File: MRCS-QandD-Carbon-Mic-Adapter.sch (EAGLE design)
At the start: 4 parts

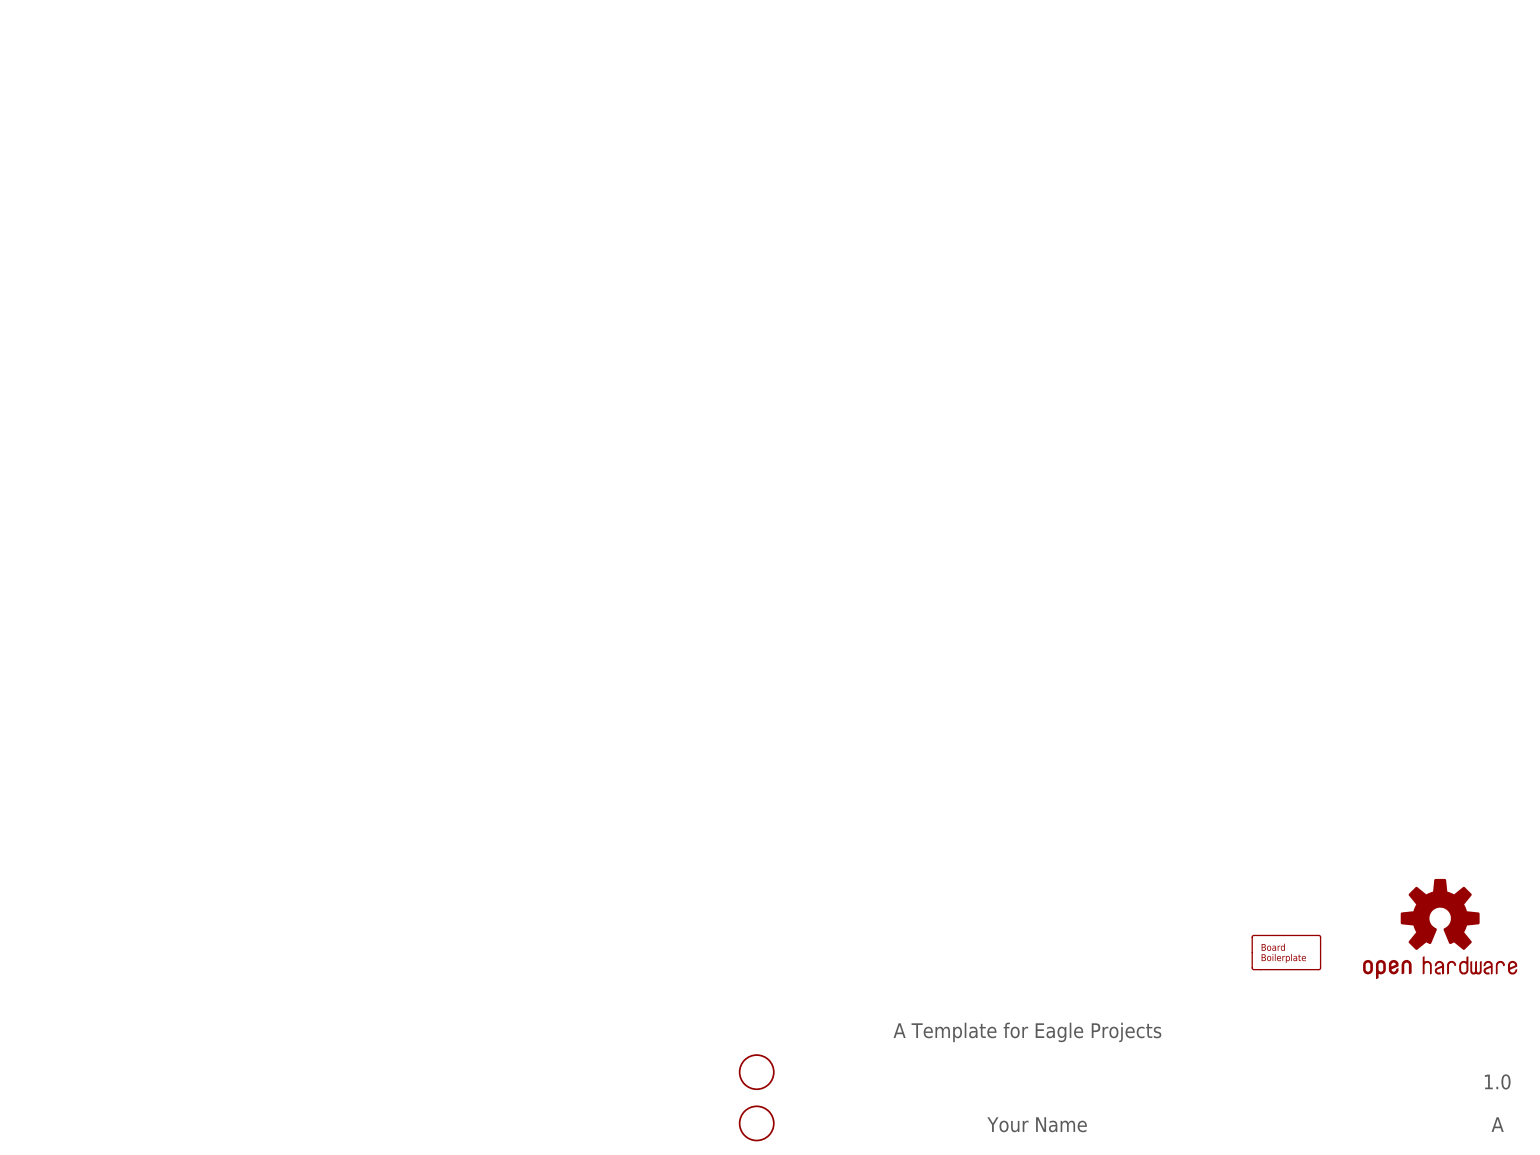
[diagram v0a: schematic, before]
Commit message: Initial design sent to PCB Fab on 1/2/22
First pass board, easier to make the PCB than fool with a bread board.
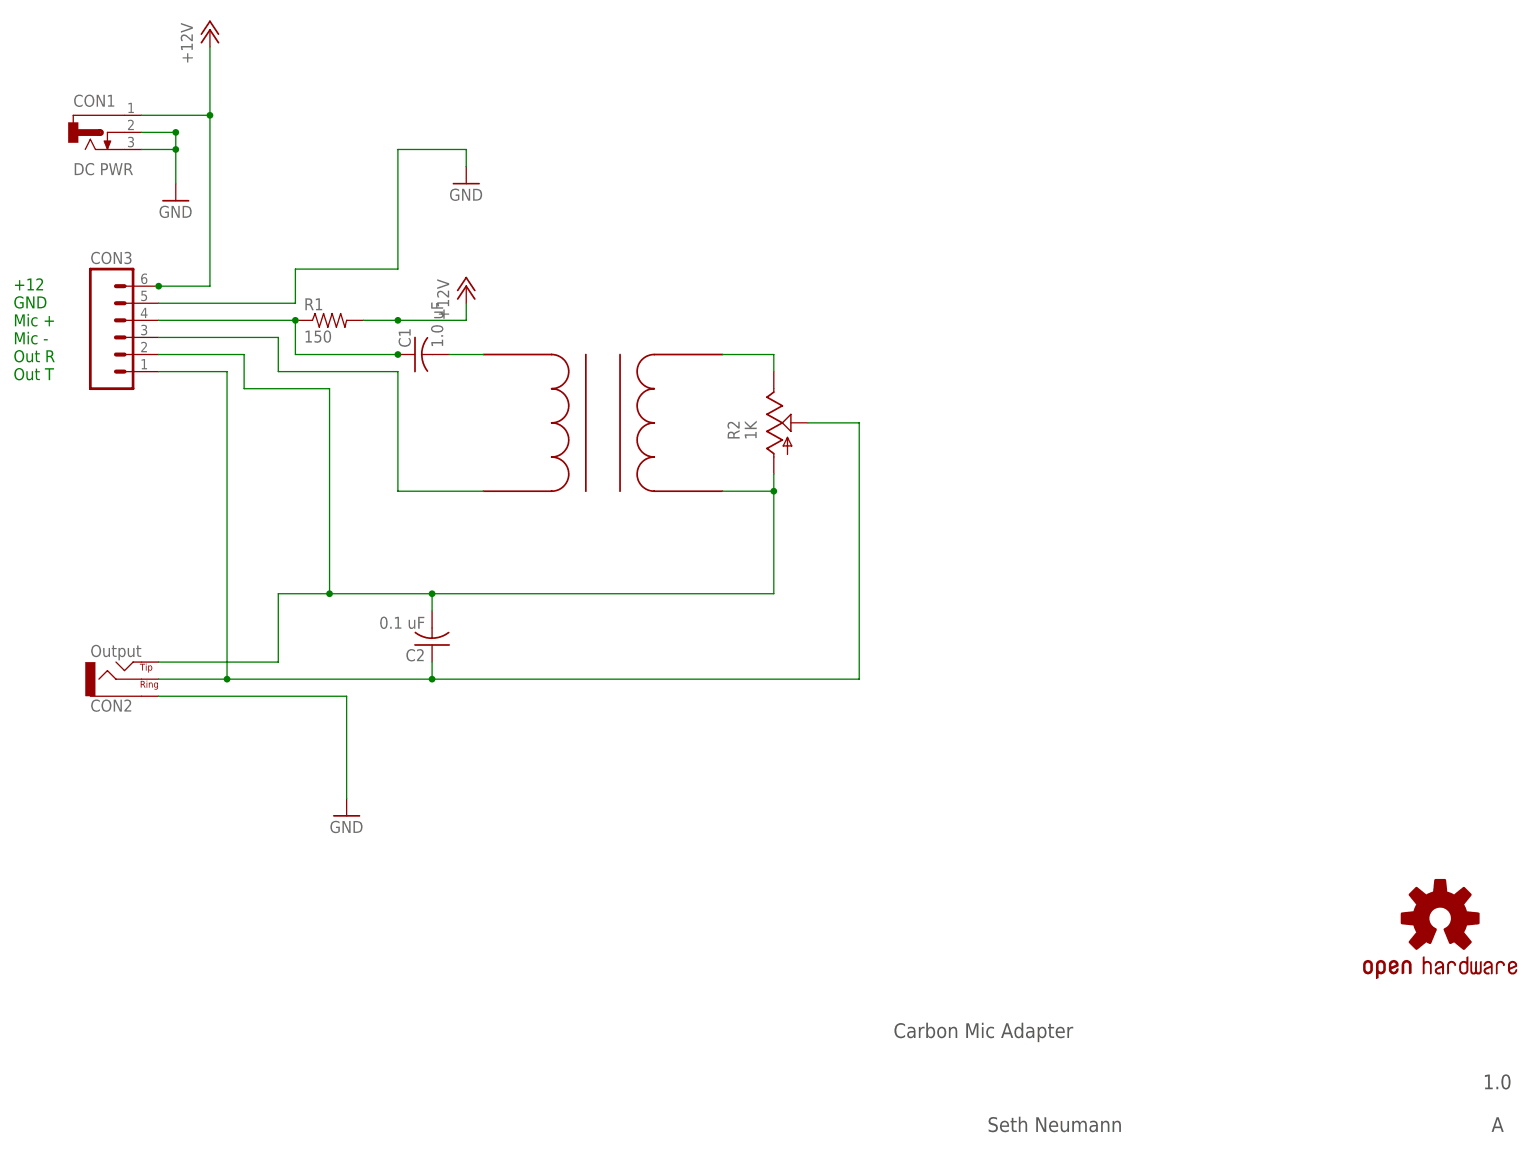
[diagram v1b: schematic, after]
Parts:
- removed BOARD1: BOARD80X100, SPCoast:BOARD80X100
- removed FID1, FID2: FIDUCIAL, SPCoast:FIDUCIAL
- added C1: 1.0 uF, SPCoast:CAPPTH2
- added C2: 0.1 uF, SPCoast:CAPPTH2
- added CON1: DC PWR, SPCoast:CONNECTOR-DC-POWER-RA
- added CON2: Output, SPCoast:CONNECTOR-AUDIO3.5MM-ADAMTECH
- added CON3: (no value), SPCoast:CONNECTOR-M063.5MM-6
- added R1: 150, SPCoast:RPTH04
- added R2: 1K, pot:TRIM_US-RS3
- added U$1: EI14_600-600, MRCS:EI14_600-600
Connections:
- new net +12V: CON1.1, CON3.6, R1.2
- new net GND: CON1.2, CON1.3, CON2.SLEEVE, CON3.5
- new net MIC+: C1.1, CON3.4, R1.1
- new net N$1: R2.E, U$1.STOP
- new net N$3: C1.2, U$1.PTOP
- new net N$7: C2.1, CON2.RING, CON3.1, R2.S
- new net OUTR: CON3.3, U$1.PBOTTOM
- new net OUTT: C2.2, CON2.TIP, CON3.2, R2.A, U$1.SBOTTOM
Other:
- note added: "+12 GND Mic + Mic - Out R Out T"
- note added: "Carbon Mic Adapter"
- note added: "Seth Neumann"
- note removed: "A Template for Eagle Projects"
- note removed: "Your Name"
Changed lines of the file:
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@@
 </classes>
 <parts>
-<part name="FRAME1" library="SPCoast" deviceset="DOC-FRAME-LETTER" device=""/>
+<part name="FRAME1" library="SPCoast" deviceset="DOC-FRAME-LETTER" device="" value="frame"/>
 <part name="OSHW1" library="SPCoast" deviceset="DOC-OSHW-LOGO-" device="M"/>
-<part name="BOARD1" library="SPCoast" deviceset="BOARD" device="80X100"/>
-<part name="FID2" library="SPCoast" deviceset="FIDUCIAL" device=""/>
-<part name="FID1" library="SPCoast" deviceset="FIDUCIAL" device=""/>
+<part name="P+1" library="SPCoast" deviceset="+12V" device=""/>
+<part name="C1" library="SPCoast" deviceset="CAP*" device="PTH2" value="1.0 uF"/>
+<part name="GND1" library="SPCoast" deviceset="GND" device=""/>
+<part name="R1" library="SPCoast" deviceset="R*" device="PTH04" value="150"/>
+<part name="CON2" library="SPCoast" deviceset="CONNECTOR-AUDIO" device="3.5MM-ADAMTECH" value="Output"/>
+<part name="U$1" library="MRCS" deviceset="EI14_600-600" device=""/>
+<part name="CON3" library="SPCoast" deviceset="CONNECTOR-M06" device="3.5MM-6"/>
+<part name="CON1" library="SPCoast" deviceset="CONNECTOR-DC-POWER" device="-RA" value="DC PWR"/>
+<part name="GND2" library="SPCoast" deviceset="GND" device=""/>
+<part name="GND3" library="SPCoast" deviceset="GND" device=""/>
+<part name="P+2" library="SPCoast" deviceset="+12V" device=""/>
+<part name="R2" library="pot" deviceset="TRIM_US-" device="RS3" value="1K"/>
+<part name="C2" library="SPCoast" deviceset="CAP*" device="PTH2" value="0.1 uF"/>
 </parts>
 <sheets>
 <sheet>
 <plain>
-<text x="152.4" y="20.32" size="2.1844" layer="97">A Template for Eagle Projects</text>
+<text x="152.4" y="20.32" size="2.1844" layer="97">Carbon Mic Adapter</text>
 <text x="240.03" y="12.7" size="2.1844" layer="97">1.0</text>
 <text x="241.3" y="6.35" size="2.1844" layer="97">A</text>
-<text x="166.37" y="6.35" size="2.1844" layer="97">Your Name</text>
+<text x="166.37" y="6.35" size="2.1844" layer="97">Seth Neumann</text>
+<text x="21.59" y="118.11" size="1.778" layer="91">+12
+GND
+Mic +
+Mic -
+Out R
+Out T</text>
 </plain>
 <instances>
@@
 <instance part="FRAME1" gate="FRAME_CONTENT" x="147.32" y="0"/>
 <instance part="OSHW1" gate="DOC-OSHW-LOGO" x="233.68" y="38.1"/>
-<instance part="BOARD1" gate="B" x="210.82" y="33.02"/>
-<instance part="FID2" gate="G$1" x="132.08" y="7.62"/>
-<instance part="FID1" gate="G$1" x="132.08" y="15.24"/>
+<instance part="P+1" gate="1" x="50.8" y="170.18"/>
+<instance part="C1" gate="C1" x="81.28" y="121.92" rot="R90"/>
+<instance part="GND1" gate="1" x="88.9" y="147.32"/>
+<instance part="R1" gate="R" x="68.58" y="127"/>
+<instance part="CON2" gate="J" x="38.1" y="73.66" rot="MR180"/>
+<instance part="U$1" gate="G$1" x="109.22" y="111.76"/>
+<instance part="CON3" gate="J" x="38.1" y="124.46"/>
+<instance part="CON1" gate="J" x="33.02" y="154.94"/>
+<instance part="GND2" gate="1" x="45.72" y="144.78"/>
+<instance part="GND3" gate="1" x="71.12" y="53.34"/>
+<instance part="P+2" gate="1" x="88.9" y="132.08"/>
+<instance part="R2" gate="G$1" x="134.62" y="111.76"/>
+<instance part="C2" gate="C1" x="83.82" y="78.74" rot="R180"/>
 </instances>
 <busses>
 </busses>
 <nets>
+<net name="+12V" class="0">
+<segment>
+<pinref part="P+1" gate="1" pin="+12V"/>
+<pinref part="CON3" gate="J" pin="6"/>
+<wire x1="43.18" y1="132.08" x2="50.8" y2="132.08" width="0.6096" layer="91"/>
+<wire x1="50.8" y1="132.08" x2="50.8" y2="157.48" width="0.6096" layer="91"/>
+<junction x="43.18" y="132.08"/>
+<pinref part="CON1" gate="J" pin="1"/>
+<wire x1="50.8" y1="157.48" x2="50.8" y2="167.64" width="0.6096" layer="91"/>
+<wire x1="40.64" y1="157.48" x2="50.8" y2="157.48" width="0.6096" layer="91"/>
+<junction x="50.8" y="157.48"/>
+</segment>
+<segment>
+<pinref part="R1" gate="R" pin="2"/>
+<wire x1="73.66" y1="127" x2="88.9" y2="127" width="0.4064" layer="91"/>
+<pinref part="P+2" gate="1" pin="+12V"/>
+<wire x1="88.9" y1="127" x2="88.9" y2="129.54" width="0.4064" layer="91"/>
+<junction x="78.74" y="127"/>
+</segment>
+</net>
+<net name="GND" class="0">
+<segment>
+<pinref part="CON1" gate="J" pin="3"/>
+<pinref part="GND2" gate="1" pin="GND"/>
+<wire x1="40.64" y1="152.4" x2="45.72" y2="152.4" width="0.6096" layer="91"/>
+<wire x1="45.72" y1="152.4" x2="45.72" y2="147.32" width="0.6096" layer="91"/>
+<pinref part="CON1" gate="J" pin="2"/>
+<wire x1="40.64" y1="154.94" x2="45.72" y2="154.94" width="0.6096" layer="91"/>
+<wire x1="45.72" y1="154.94" x2="45.72" y2="152.4" width="0.6096" layer="91"/>
+<junction x="45.72" y="152.4"/>
+<junction x="45.72" y="154.94"/>
+</segment>
+<segment>
+<wire x1="43.18" y1="71.12" x2="71.12" y2="71.12" width="0.6096" layer="91"/>
+<pinref part="CON2" gate="J" pin="SLEEVE"/>
+<pinref part="GND3" gate="1" pin="GND"/>
+<wire x1="71.12" y1="71.12" x2="71.12" y2="55.88" width="0.6096" layer="91"/>
+</segment>
+<segment>
+<wire x1="78.74" y1="134.62" x2="78.74" y2="152.4" width="0.6096" layer="91"/>
+<wire x1="78.74" y1="152.4" x2="88.9" y2="152.4" width="0.6096" layer="91"/>
+<pinref part="GND1" gate="1" pin="GND"/>
+<wire x1="88.9" y1="152.4" x2="88.9" y2="149.86" width="0.6096" layer="91"/>
+<pinref part="CON3" gate="J" pin="5"/>
+<wire x1="43.18" y1="129.54" x2="63.5" y2="129.54" width="0.6096" layer="91"/>
+<wire x1="63.5" y1="129.54" x2="63.5" y2="134.62" width="0.6096" layer="91"/>
+<wire x1="63.5" y1="134.62" x2="78.74" y2="134.62" width="0.6096" layer="91"/>
+</segment>
+</net>
+<net name="MIC+" class="0">
+<segment>
+<pinref part="R1" gate="R" pin="1"/>
+<pinref part="CON3" gate="J" pin="4"/>
+<wire x1="63.5" y1="127" x2="43.18" y2="127" width="0.4064" layer="91"/>
+<wire x1="63.5" y1="127" x2="63.5" y2="121.92" width="0.4064" layer="91"/>
+<wire x1="63.5" y1="121.92" x2="78.74" y2="121.92" width="0.4064" layer="91"/>
+<pinref part="C1" gate="C1" pin="1"/>
+<junction x="63.5" y="127"/>
+<junction x="78.74" y="121.92"/>
+</segment>
+</net>
+<net name="N$3" class="0">
+<segment>
+<pinref part="C1" gate="C1" pin="2"/>
+<pinref part="U$1" gate="G$1" pin="PTOP"/>
+<wire x1="86.36" y1="121.92" x2="91.44" y2="121.92" width="0.4064" layer="91"/>
+</segment>
+</net>
+<net name="OUTR" class="0">
+<segment>
+<pinref part="CON3" gate="J" pin="3"/>
+<wire x1="43.18" y1="124.46" x2="60.96" y2="124.46" width="0.6096" layer="91"/>
+<wire x1="60.96" y1="124.46" x2="60.96" y2="119.38" width="0.6096" layer="91"/>
+<wire x1="60.96" y1="119.38" x2="78.74" y2="119.38" width="0.6096" layer="91"/>
+<wire x1="78.74" y1="119.38" x2="78.74" y2="101.6" width="0.6096" layer="91"/>
+<pinref part="U$1" gate="G$1" pin="PBOTTOM"/>
+<wire x1="78.74" y1="101.6" x2="91.44" y2="101.6" width="0.6096" layer="91"/>
+</segment>
+</net>
+<net name="N$1" class="0">
+<segment>
+<pinref part="U$1" gate="G$1" pin="STOP"/>
+<pinref part="R2" gate="G$1" pin="E"/>
+<wire x1="127" y1="121.92" x2="134.62" y2="121.92" width="0.4064" layer="91"/>
+<wire x1="134.62" y1="121.92" x2="134.62" y2="119.38" width="0.4064" layer="91"/>
+</segment>
+</net>
+<net name="OUTT" class="0">
+<segment>
+<pinref part="U$1" gate="G$1" pin="SBOTTOM"/>
+<pinref part="R2" gate="G$1" pin="A"/>
+<wire x1="127" y1="101.6" x2="134.62" y2="101.6" width="0.4064" layer="91"/>
+<wire x1="134.62" y1="101.6" x2="134.62" y2="104.14" width="0.4064" layer="91"/>
+<pinref part="CON2" gate="J" pin="TIP"/>
+<wire x1="43.18" y1="76.2" x2="60.96" y2="76.2" width="0.4064" layer="91"/>
+<wire x1="60.96" y1="76.2" x2="60.96" y2="86.36" width="0.4064" layer="91"/>
+<wire x1="60.96" y1="86.36" x2="68.58" y2="86.36" width="0.4064" layer="91"/>
+<wire x1="68.58" y1="86.36" x2="83.82" y2="86.36" width="0.4064" layer="91"/>
+<wire x1="83.82" y1="86.36" x2="134.62" y2="86.36" width="0.4064" layer="91"/>
+<wire x1="134.62" y1="86.36" x2="134.62" y2="101.6" width="0.4064" layer="91"/>
+<pinref part="CON3" gate="J" pin="2"/>
+<wire x1="43.18" y1="121.92" x2="55.88" y2="121.92" width="0.4064" layer="91"/>
+<wire x1="55.88" y1="121.92" x2="55.88" y2="116.84" width="0.4064" layer="91"/>
+<wire x1="55.88" y1="116.84" x2="68.58" y2="116.84" width="0.4064" layer="91"/>
+<wire x1="68.58" y1="116.84" x2="68.58" y2="86.36" width="0.4064" layer="91"/>
+<junction x="68.58" y="86.36"/>
+<junction x="134.62" y="101.6"/>
+<pinref part="C2" gate="C1" pin="2"/>
+<wire x1="83.82" y1="83.82" x2="83.82" y2="86.36" width="0.4064" layer="91"/>
+<junction x="83.82" y="86.36"/>
+</segment>
+</net>
+<net name="N$7" class="0">
+<segment>
+<pinref part="CON2" gate="J" pin="RING"/>
+<wire x1="43.18" y1="73.66" x2="53.34" y2="73.66" width="0.4064" layer="91"/>
+<wire x1="53.34" y1="73.66" x2="83.82" y2="73.66" width="0.4064" layer="91"/>
+<wire x1="83.82" y1="73.66" x2="147.32" y2="73.66" width="0.4064" layer="91"/>
+<wire x1="147.32" y1="73.66" x2="147.32" y2="111.76" width="0.4064" layer="91"/>
+<pinref part="R2" gate="G$1" pin="S"/>
+<wire x1="147.32" y1="111.76" x2="139.7" y2="111.76" width="0.4064" layer="91"/>
+<pinref part="CON3" gate="J" pin="1"/>
+<wire x1="43.18" y1="119.38" x2="53.34" y2="119.38" width="0.4064" layer="91"/>
+<wire x1="53.34" y1="119.38" x2="53.34" y2="73.66" width="0.4064" layer="91"/>
+<junction x="53.34" y="73.66"/>
+<pinref part="C2" gate="C1" pin="1"/>
+<wire x1="83.82" y1="76.2" x2="83.82" y2="73.66" width="0.4064" layer="91"/>
+<junction x="83.82" y="73.66"/>
+</segment>
+</net>
 </nets>
 </sheet>
